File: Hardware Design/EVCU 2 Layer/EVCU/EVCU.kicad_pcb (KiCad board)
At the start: 2 copper layers, 80.3 x 86.8 mm, 82 parts, among them J1 Conn_01x06, J2 Conn_01x02, J3 APPS/BSE_Conn, J4 Micro_SD_Card, J5 DB9_Male, J6 Conn_01x02, Q1 Q_PMOS_GSD, U1 AZ1117-3.3, U10 EMIF06-MSD02N16, U11 ESDALC6V1W5, U2 AP62250WU-7, U3 STM32L4R9ZITx, U4 LMV321, U5 MPU-6500, U6 SN65HVD230, U7 LMV321, U8 LMV321, U9 ESDCAN24-2BLY, X1 ECS-2520MV-160-CN-TR

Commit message: wire
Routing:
- net /NRST: track 36.5 -> 36.6 mm, vias 1 -> 2
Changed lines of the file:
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@@
   (segment (start 129.516324 83.9046) (end 128.7817 83.9046) (width 0.3) (layer "F.Cu") (net 6))
   (segment (start 130.5814 84.969676) (end 129.516324 83.9046) (width 0.3) (layer "F.Cu") (net 6))
+  (segment (start 137.9982 87.6046) (end 131.8768 81.4832) (width 0.3) (layer "F.Cu") (net 7))
   (segment (start 108.6598 80.9046) (end 109.1784 81.4232) (width 0.3) (layer "F.Cu") (net 7))
   (segment (start 105.7229 81.1692) (end 105.9875 80.9046) (width 0.3) (layer "F.Cu") (net 7))
   (segment (start 105.9875 80.9046) (end 107.4567 80.9046) (width 0.3) (layer "F.Cu") (net 7))
+  (segment (start 139.319 87.6046) (end 137.9982 87.6046) (width 0.3) (layer "F.Cu") (net 7))
+  (segment (start 131.8768 81.4832) (end 131.8168 81.4232) (width 0.3) (layer "F.Cu") (net 7))
   (segment (start 107.4567 80.9046) (end 108.6598 80.9046) (width 0.3) (layer "F.Cu") (net 7))
+  (via (at 131.8768 81.4832) (size 0.6) (drill 0.3) (layers "F.Cu" "B.Cu") (net 7))
   (via (at 109.1784 81.4232) (size 0.6) (drill 0.3) (layers "F.Cu" "B.Cu") (net 7))
-  (segment (start 137.9982 87.6046) (end 131.8168 81.4232) (width 0.3) (layer "B.Cu") (net 7))
-  (segment (start 139.319 87.6046) (end 137.9982 87.6046) (width 0.3) (layer "B.Cu") (net 7))
+  (segment (start 131.8768 81.4832) (end 131.8168 81.4232) (width 0.3) (layer "B.Cu") (net 7))
   (segment (start 131.8168 81.4232) (end 109.1784 81.4232) (width 0.3) (layer "B.Cu") (net 7))
   (segment (start 121.7281 97.1172) (end 121.6141 97.2312) (width 0.2) (layer "F.Cu") (net 8))

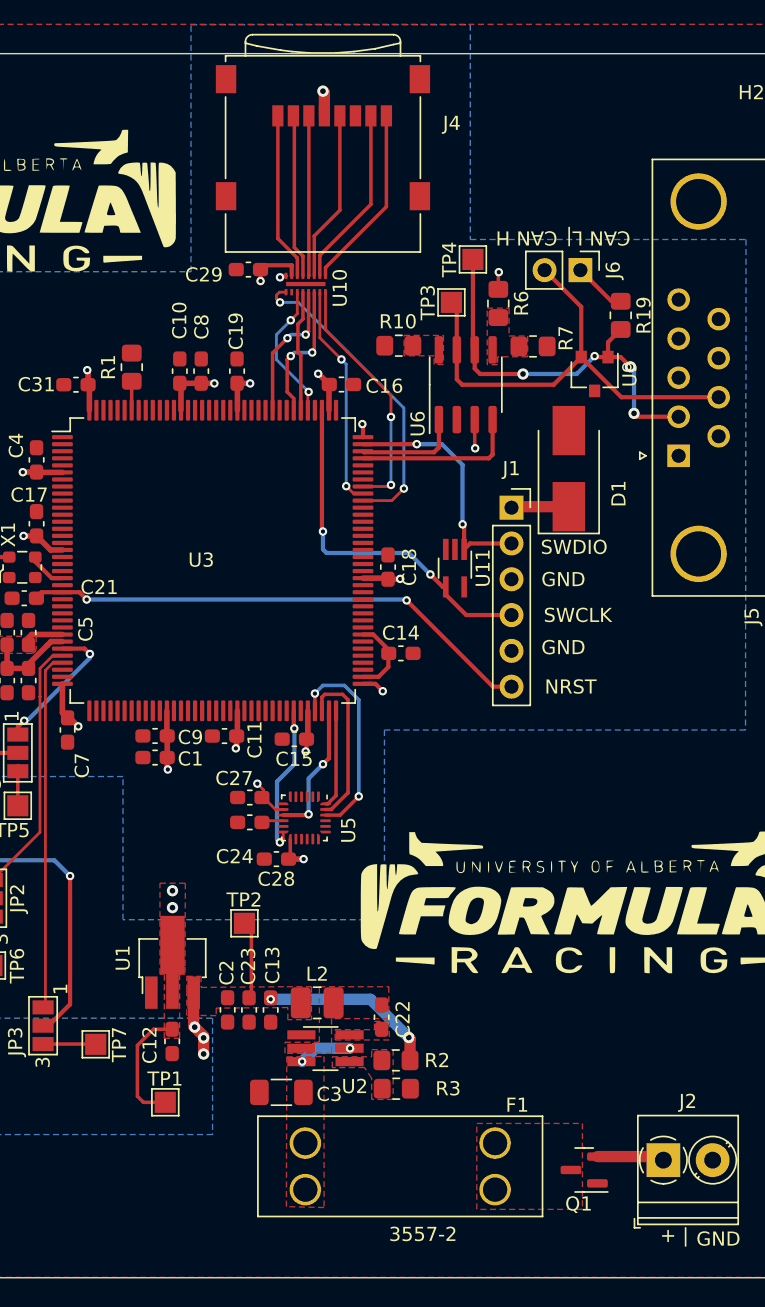
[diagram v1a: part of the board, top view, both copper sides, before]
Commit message: moving vias from pads
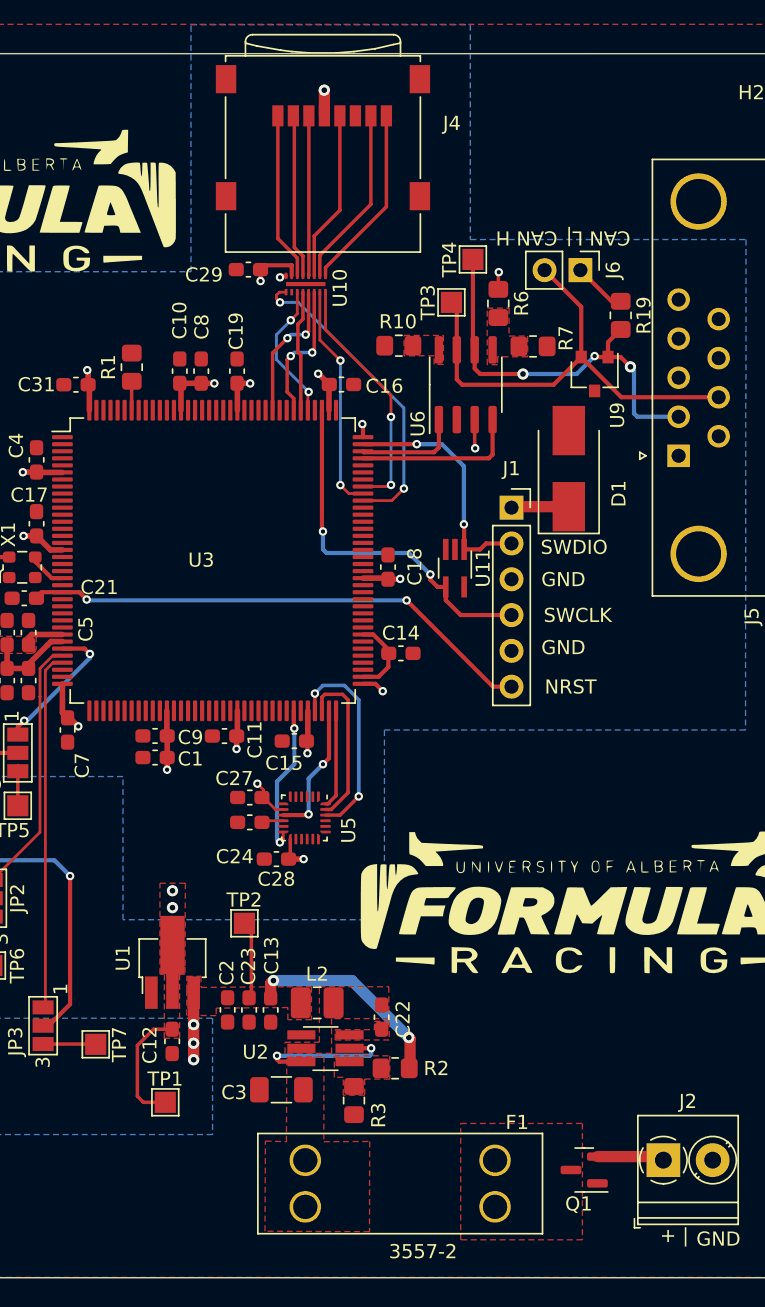
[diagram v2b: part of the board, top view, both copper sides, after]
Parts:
- moved R3 3.12 mm to (128.1, 117.0), turned to -90 degrees
- moved F1 1.22 mm to (138.2, 124.5)
- moved R2 0.57 mm to (131.1, 114.7)
- moved C3 0.18 mm to (123.0, 116.2)
- moved C15 0.14 mm to (123.9, 91.5)
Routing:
- net +BATT: track 3.79 -> 10.7 mm
- net +5V: track 25.2 -> 26.9 mm
- net /CAN_L: vias 4 -> 3

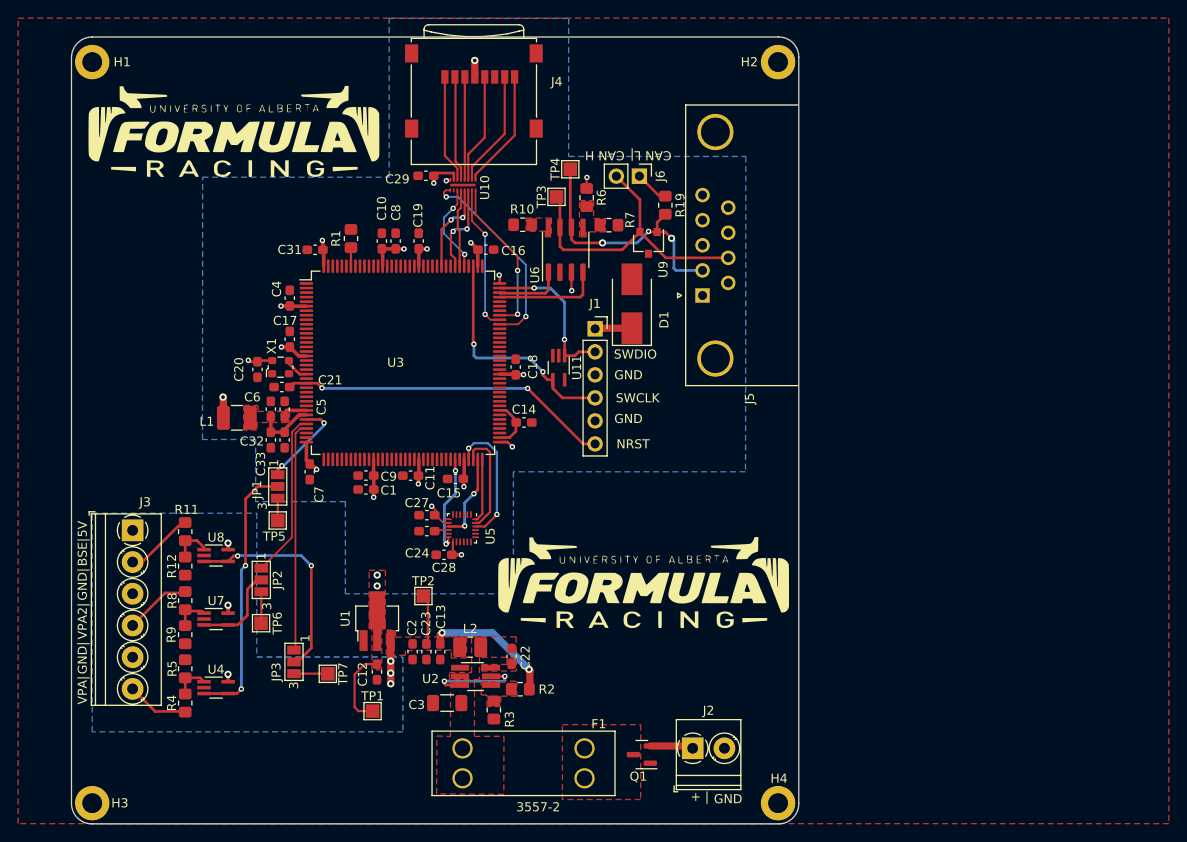
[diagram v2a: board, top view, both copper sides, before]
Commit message: increasing net clearance, changing trace angles, decreasing trace-to-pad width
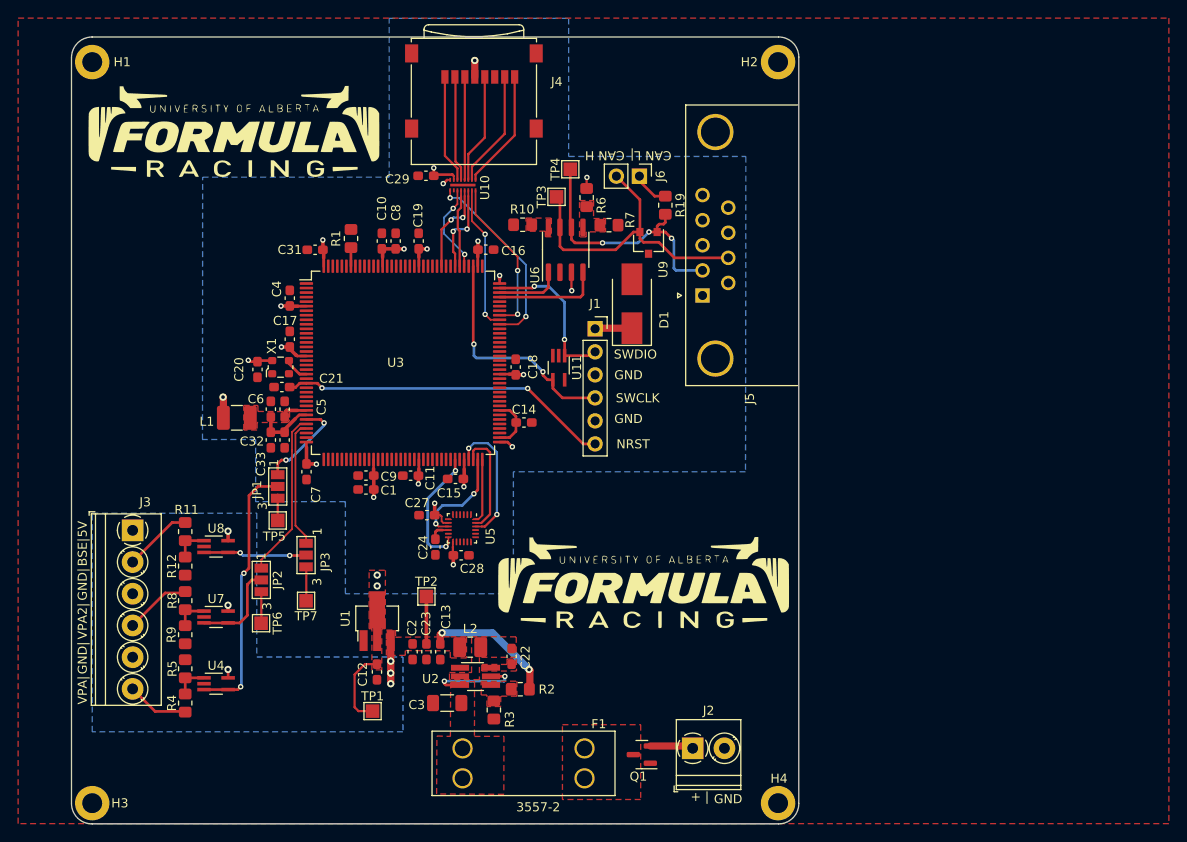
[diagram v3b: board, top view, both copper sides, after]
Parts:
- moved JP3 11.9 mm to (107.4, 99.9)
- moved TP7 8.41 mm to (107.4, 104.9), turned to 180 degrees
- moved C24 1.99 mm to (121.7, 99.0), turned to -90 degrees
- moved C28 1.90 mm to (124.5, 99.9), turned to 0 degrees
- moved U8 0.99 mm to (97.5, 98.9)
- moved U4 0.43 mm to (97.5, 114.1)
- moved C7 0.36 mm to (107.5, 90.7)
- moved TP2 0.33 mm to (120.7, 104.4)
- moved U7 0.23 mm to (97.5, 106.7)
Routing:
- net /LMVCOUT: track 24.2 -> 11.4 mm
- net /VOUT_BSE: track 25.2 -> 14.0 mm
- net /INT: track 10.8 -> 13.8 mm
- net /MISO: track 9.77 -> 11.8 mm
- net /MCU_CD: track 22.2 -> 21.2 mm
- net Net-(C24-Pad1): track 1.55 -> 2.32 mm
- net +3V3: track 71.1 -> 71.7 mm
- net /LMA+_BSE: track 4.58 -> 4.04 mm
